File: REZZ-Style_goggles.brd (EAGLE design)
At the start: 65.5 x 65.5 mm, 80 parts

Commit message: second ring completed
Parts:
- removed U$1: (no value), NeoPixelRing:ADAFRUIT_5MM
- moved C25 6.80 mm to (29.3, 54.5), turned to 101.3 degrees
- moved C38 6.20 mm to (14.0, 39.4), turned to 168.8 degrees
- moved C30 6.02 mm to (51.9, 31.9), turned to 348.8 degrees
- moved C26 5.94 mm to (36.8, 54.5), turned to 78.8 degrees
- moved C36 5.91 mm to (16.9, 24.7), turned to 213.8 degrees
- moved C29 5.87 mm to (52.0, 39.3), turned to 11.3 degrees
- moved C31 5.78 mm to (49.1, 24.9), turned to 326.3 degrees
- moved C39 5.74 mm to (16.9, 46.3), turned to 146.3 degrees
- moved C27 5.67 mm to (43.8, 51.7), turned to 56.3 degrees
- moved C37 5.66 mm to (14.0, 31.7), turned to 191.3 degrees
- moved C28 5.30 mm to (49.0, 46.3), turned to 33.8 degrees
- moved C35 5.22 mm to (22.1, 19.5), turned to 236.3 degrees
- moved C34 5.17 mm to (29.2, 16.6), turned to 258.8 degrees
- moved C40 5.04 mm to (22.3, 51.5), turned to 123.8 degrees
- moved C33 4.98 mm to (36.8, 16.8), turned to 281.3 degrees
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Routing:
- net VDD: track 0.00 -> 40.7 mm, vias 24 -> 42
- net N$24: track 1.37 -> 16.8 mm, vias 1 -> 2
- net N$28: track 0.00 -> 7.36 mm, vias 0 -> 2
- net N$40: track 0.00 -> 7.35 mm, vias 0 -> 2
- net N$41: track 0.00 -> 7.33 mm, vias 0 -> 2
- net N$31: track 0.00 -> 7.28 mm, vias 0 -> 2
- net N$38: track 0.00 -> 7.27 mm, vias 0 -> 2
- net N$30: track 0.00 -> 7.26 mm, vias 0 -> 2
- net N$33: track 0.00 -> 7.25 mm, vias 0 -> 2
- net N$39: track 0.00 -> 7.23 mm, vias 0 -> 2
- net N$36: track 0.00 -> 7.23 mm, vias 0 -> 2
- net N$32: track 0.00 -> 7.19 mm, vias 0 -> 2
- net N$35: track 0.00 -> 7.17 mm, vias 0 -> 2
- net N$27: track 0.00 -> 7.09 mm, vias 0 -> 3
- net N$34: track 0.00 -> 7.07 mm, vias 0 -> 2
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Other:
- board text removed: "NeoPixel Ring x24"

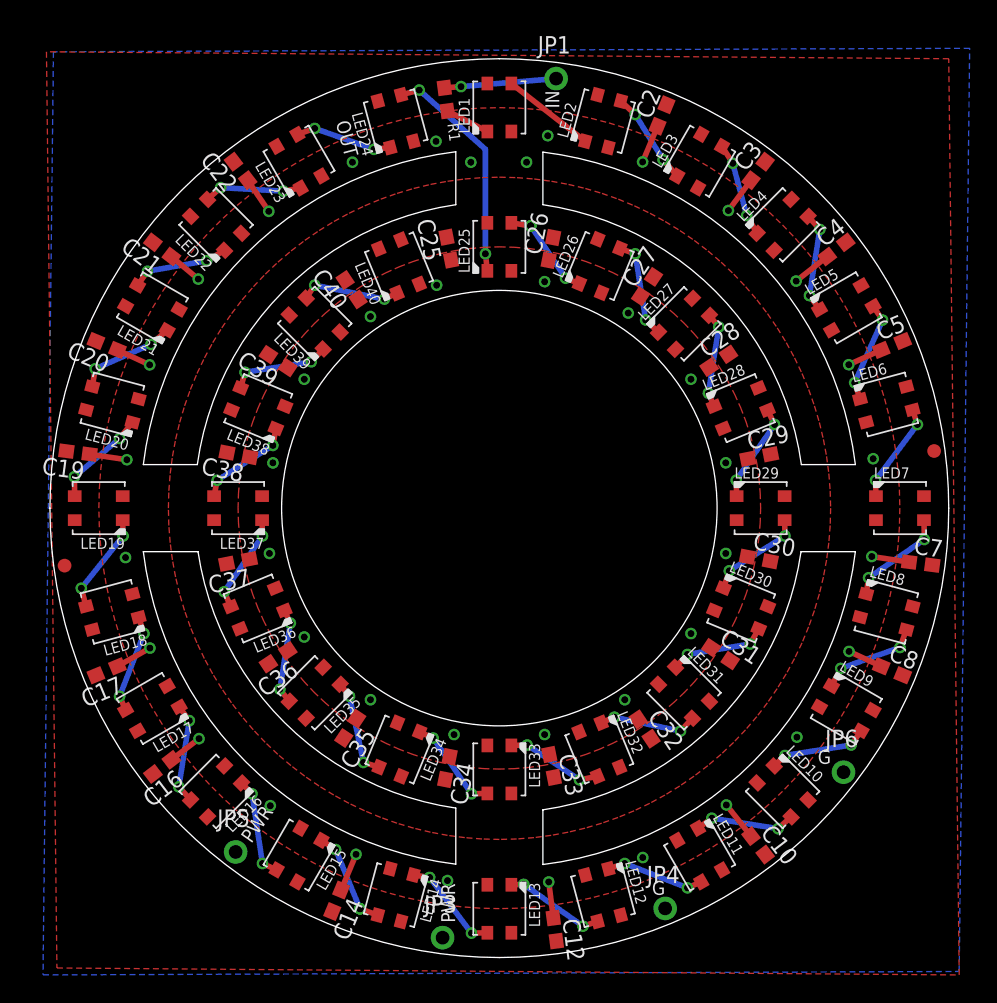
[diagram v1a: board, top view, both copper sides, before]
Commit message: trace adjustments
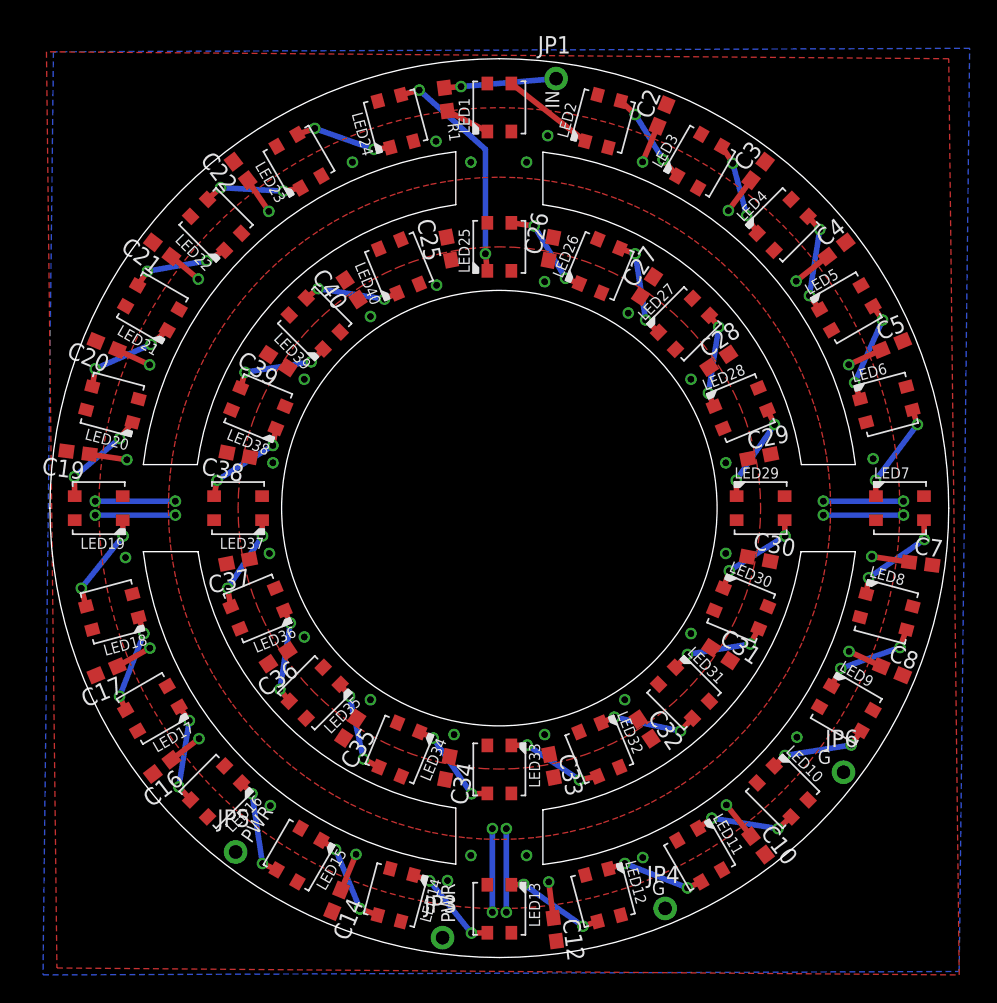
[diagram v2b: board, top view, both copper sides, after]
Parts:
- removed FID1, FID2: FIDUCIAL"", microbuilder:FIDUCIAL_1MM
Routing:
- net GND: track 0.00 -> 35.6 mm, vias 0 -> 12
- net N$27: track 7.09 -> 7.21 mm, vias 3 -> 2
- net VDD: vias 42 -> 44
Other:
- board text removed: "OUT"
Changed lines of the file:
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@@
 <wire x1="33.02" y1="2.794" x2="0.254" y2="35.56" width="0" layer="20" curve="-90"/>
 <text x="36.3728" y="66.0146" size="1.016" layer="21" ratio="10" rot="R270">IN</text>
-<text x="21.082" y="63.6778" size="1.016" layer="21" ratio="10" rot="R285">OUT</text>
 <text x="44.1452" y="7.366" size="1.016" layer="21" ratio="10">G</text>
 <text x="29.7942" y="5.334" size="1.016" layer="21" ratio="10" rot="R90">PWR</text>
@@
 <element name="C22" library="rcl" package="C0603" value="" x="14.155675" y="60.14440625" rot="R127.5"/>
 <element name="JP1" library="NeoPixelRing" package="1X01-CLEANBIG" value="" x="37.1602" y="66.8782"/>
-<element name="FID1" library="microbuilder" package="FIDUCIAL_1MM" value="FIDUCIAL&quot;&quot;" x="1.3208" y="31.369">
-<attribute name="BOM" value="EXCLUDE" x="1.3208" y="31.369" size="1.778" layer="27" display="off"/>
-</element>
-<element name="FID2" library="microbuilder" package="FIDUCIAL_1MM" value="FIDUCIAL&quot;&quot;" x="64.7192" y="39.7256">
-<attribute name="BOM" value="EXCLUDE" x="64.7192" y="39.7256" size="1.778" layer="27" display="off"/>
-</element>
 <element name="JP5" library="NeoPixelRing" package="1X01-CLEANBIG" value="" x="13.7922" y="10.4902"/>
 <element name="JP6" library="NeoPixelRing" package="1X01-CLEANBIG" value="" x="58.1152" y="16.3068"/>
@@
 <vertex x="33.02" y="11.4046" curve="-90.060282"/>
 </polygon>
-<wire x1="2.06" y1="34.685" x2="12.22" y2="34.685" width="0" layer="19" extent="1-1"/>
+<via x="32.512" y="12.192" extent="1-16" drill="0.5"/>
+<via x="33.528" y="12.192" extent="1-16" drill="0.5"/>
+<via x="32.512" y="6.096" extent="1-16" drill="0.5"/>
+<via x="33.528" y="6.096" extent="1-16" drill="0.5"/>
+<wire x1="32.512" y1="12.192" x2="32.512" y2="6.096" width="0.4064" layer="16"/>
+<wire x1="33.528" y1="12.192" x2="33.528" y2="6.096" width="0.4064" layer="16"/>
+<via x="56.642" y="35.052" extent="1-16" drill="0.5"/>
+<via x="56.642" y="36.068" extent="1-16" drill="0.5"/>
+<via x="62.484" y="36.068" extent="1-16" drill="0.5"/>
+<via x="62.484" y="35.052" extent="1-16" drill="0.5"/>
+<wire x1="56.642" y1="36.068" x2="62.484" y2="36.068" width="0.4064" layer="16"/>
+<wire x1="56.642" y1="35.052" x2="62.484" y2="35.052" width="0.4064" layer="16"/>
+<via x="9.398" y="36.068" extent="1-16" drill="0.5"/>
+<via x="9.398" y="35.052" extent="1-16" drill="0.5"/>
+<via x="3.556" y="35.052" extent="1-16" drill="0.5"/>
+<via x="3.556" y="36.068" extent="1-16" drill="0.5"/>
+<wire x1="3.556" y1="36.068" x2="9.398" y2="36.068" width="0.4064" layer="16"/>
+<wire x1="9.398" y1="35.052" x2="3.556" y2="35.052" width="0.4064" layer="16"/>
 </signal>
 <signal name="VDD">
@@
 <via x="30.942025" y="60.782453125" extent="1-16" drill="0.5"/>
 <via x="35.006025" y="60.782453125" extent="1-16" drill="0.5"/>
+<via x="30.942025" y="10.236453125" extent="1-16" drill="0.5"/>
+<via x="35.006025" y="10.236453125" extent="1-16" drill="0.5"/>
 </signal>
 <signal name="N$12">
@@
 <contactref element="LED14" pad="1"/>
 <via x="30.988" y="4.572" extent="1-16" drill="0.5"/>
-<via x="27.94" y="8.636" extent="1-16" drill="0.5"/>
-<wire x1="30.988" y1="4.572" x2="27.94" y2="8.636" width="0.4064" layer="16"/>
+<via x="27.94" y="8.382" extent="1-16" drill="0.5"/>
+<wire x1="30.988" y1="4.572" x2="27.94" y2="8.382" width="0.4064" layer="16"/>
 <wire x1="32.145" y1="4.6" x2="30.988" y2="4.572" width="0.4064" layer="1"/>
-<wire x1="27.94" y1="8.636" x2="26.758059375" y2="8.809328125" width="0.4064" layer="1"/>
+<wire x1="27.94" y1="8.382" x2="26.758059375" y2="8.809328125" width="0.4064" layer="1"/>
 </signal>
 <signal name="N$14">
@@
 <contactref element="LED25" pad="3"/>
 <contactref element="LED26" pad="1"/>
-<via x="35.306" y="56.134" extent="1-16" drill="0.5"/>
-<wire x1="33.895" y1="56.36" x2="35.306" y2="56.134" width="0.4064" layer="1"/>
-<via x="35.306" y="56.134" extent="1-16" drill="0.5"/>
+<wire x1="33.895" y1="56.36" x2="35.56" y2="56.134" width="0.4064" layer="1"/>
+<via x="35.56" y="56.134" extent="1-16" drill="0.5"/>
 <via x="37.846" y="52.324" extent="1-16" drill="0.5"/>
 <wire x1="38.857109375" y1="51.93105625" x2="37.846" y2="52.324" width="0.4064" layer="1"/>
-<wire x1="35.306" y1="56.134" x2="37.846" y2="52.324" width="0.4064" layer="16"/>
+<wire x1="35.56" y1="56.134" x2="37.846" y2="52.324" width="0.4064" layer="16"/>
 </signal>
 <signal name="N$28">
@@
 <contactref element="LED34" pad="3"/>
 <contactref element="LED35" pad="1"/>
-<via x="23.114" y="17.018" extent="1-16" drill="0.5"/>
+<via x="23.114" y="17.272" extent="1-16" drill="0.5"/>
 <via x="22.098" y="21.844" extent="1-16" drill="0.5"/>
-<wire x1="24.252109375" y1="16.67585625" x2="23.114" y2="17.018" width="0.4064" layer="1"/>
+<wire x1="24.252109375" y1="16.67585625" x2="23.114" y2="17.272" width="0.4064" layer="1"/>
 <wire x1="21.414153125" y1="22.716715625" x2="22.098" y2="21.844" width="0.4064" layer="1"/>
-<wire x1="23.114" y1="17.018" x2="22.098" y2="21.844" width="0.4064" layer="16"/>
+<wire x1="23.114" y1="17.272" x2="22.098" y2="21.844" width="0.4064" layer="16"/>
 </signal>
 <signal name="N$37">
@@
 <contactref element="LED36" pad="3"/>
 <contactref element="LED37" pad="1"/>
-<via x="12.954" y="29.464" extent="1-16" drill="0.5"/>
+<via x="13.208" y="29.718" extent="1-16" drill="0.5"/>
 <via x="15.748" y="33.528" extent="1-16" drill="0.5"/>
-<wire x1="13.4407625" y1="28.383496875" x2="12.954" y2="29.464" width="0.4064" layer="1"/>
+<wire x1="13.4407625" y1="28.383496875" x2="13.208" y2="29.718" width="0.4064" layer="1"/>
 <wire x1="15.72" y1="34.685" x2="15.748" y2="33.528" width="0.4064" layer="1"/>
-<wire x1="12.954" y1="29.464" x2="15.748" y2="33.528" width="0.4064" layer="16"/>
+<wire x1="13.208" y1="29.718" x2="15.748" y2="33.528" width="0.4064" layer="16"/>
 </signal>
 <signal name="N$39">
@@
 <contactref element="LED39" pad="3"/>
 <contactref element="LED40" pad="1"/>
-<via x="19.558" y="51.816" extent="1-16" drill="0.5"/>
+<via x="19.812" y="51.562" extent="1-16" drill="0.5"/>
 <via x="24.638" y="50.8" extent="1-16" drill="0.5"/>
-<wire x1="18.93928125" y1="50.878153125" x2="19.558" y2="51.816" width="0.4064" layer="1"/>
+<wire x1="18.93928125" y1="50.878153125" x2="19.812" y2="51.562" width="0.4064" layer="1"/>
 <wire x1="25.5661" y1="51.2359625" x2="24.638" y2="50.8" width="0.4064" layer="1"/>
-<wire x1="19.558" y1="51.816" x2="24.638" y2="50.8" width="0.4064" layer="16"/>
+<wire x1="19.812" y1="51.562" x2="24.638" y2="50.8" width="0.4064" layer="16"/>
 </signal>
 </signals>
